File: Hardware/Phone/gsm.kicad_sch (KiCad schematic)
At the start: 28 parts

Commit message: e ink is done
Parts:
- removed U5: ~, Felix_GSM:GSMM-SMD_SIM800A32M, symbol Felix_GSM:SIM800A 32m
- added C24: 100n, Capacitor_SMD:C_0603_1608Metric, symbol Device:C
- added C25, C26, C27: 22p, Capacitor_SMD:C_0603_1608Metric, symbol Device:C
- added C28: 1u, Capacitor_SMD:C_0603_1608Metric, symbol Device:C
- added C29: 1nF, Capacitor_SMD:C_1206_3216Metric, symbol Device:C
- added C30, C31: ~, Capacitor_SMD:C_0603_1608Metric, symbol Device:C
- added CARD1: ~, Felix_GSM:SIM-SMD_503960-0696, symbol Felix_GSM:503960-0696
- added D5: ESDA6V1-5W6, Package_TO_SOT_SMD:SOT-363_SC-70-6, symbol Power_Protection:ESDA6V1-5SC6
- added D6: ~, Felix:SOD-882_L1.0-W0.6-BI, symbol Felix:H5VL10B
- added F2: 500mA PTC, Fuse:Fuse_1206_3216Metric_Pad1.42x1.75mm_HandSolder, symbol Device:Fuse
- added J5: Conn_Coaxial, Connector_Coaxial:U.FL_Hirose_U.FL-R-SMT-1_Vertical, symbol Connector:Conn_Coaxial
- added J6: Conn_01x02_Socket, Connector_PinHeader_2.54mm:PinHeader_1x02_P2.54mm_Vertical, symbol Connector:Conn_01x02_Socket
- added J7: USB_C_Receptacle_USB2.0_16P, Connector_USB:USB_C_Receptacle_HRO_TYPE-C-31-M-12, symbol Connector:USB_C_Receptacle_USB2.0_16P
- added R16, R18, R19: 1K, Resistor_SMD:R_0603_1608Metric, symbol Device:R
- added R17, R20: 5k6, Resistor_SMD:R_0603_1608Metric, symbol Device:R
- added R21: 4k7, Resistor_SMD:R_0603_1608Metric, symbol Device:R
- added R22, R23, R24: 51R, Resistor_SMD:R_0603_1608Metric, symbol Device:R
- added R25: 0R, Resistor_SMD:R_0603_1608Metric, symbol Device:R
- added TP1: TestPoint, TestPoint:TestPoint_Pad_D1.0mm, symbol Connector:TestPoint
- added U5: USBLC6-2SC6, Package_TO_SOT_SMD:SOT-23-6, symbol Power_Protection:USBLC6-2SC6
- added U6: SIM800C, RF_GSM:SIMCom_SIM800C, symbol RF_GSM:SIM800C
- added U7: ~, Felix:MIC-TH_BD4.0-P1.40_KEEG1542PBL-A, symbol Felix:KEEG1542PBL-A
- R11, R12: value 1K -> 22R
- R13: value 1K -> 5k1; footprint Resistor_SMD:R_0603_1608Metric -> Resistor_SMD:R_1206_3216Metric
- R14: value 5k6 -> 5k1; footprint Resistor_SMD:R_0603_1608Metric -> Resistor_SMD:R_1206_3216Metric
- R15: value 5k6 -> 1M; footprint Resistor_SMD:R_0603_1608Metric -> Resistor_SMD:R_1206_3216Metric
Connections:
- net +4V: now also U6.34 (VBAT), U6.35 (VBAT)
- net DTR: now also R16.2; no longer R13.2
- net GND: now also R13.2, C24.1, C25.1, C26.1, C27.1, C28.1, C29.2, C30.1, C31.1, CARD1.C5 (GND), CARD1.C9 (SHEEL), D5.2 (GND), D6.2 (A), J5.2 (Ext), J7.A1 (GND), J7.A12 (GND), J7.B1 (GND), J7.B12 (GND), R17.2, R20.2, U5.2 (GND), U6.13 (GND), U6.19 (GND), U6.21 (GND), U6.27 (GND), U6.30 (GND), U6.31 (GND), U6.33 (GND), U6.36 (GND), U6.37 (GND), U6.8 (GND)
- net RX: now also R19.2; no longer R12.2
- net TX: now also R18.2; no longer R11.2
- net at C20.1, C21.1, C22.2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: now also U6.10 (MICN), U7.1
- net at C18.1, C19.1, C20.2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: now also U6.9 (MICP), U7.2
- net at R13.1: now also J7.A5 (CC1); no longer R15.1
- net at C10.1, C11.2, C14.1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: now also J6.1 (Pin_1), U6.11 (SPKP)
- net at C10.2, C12.1, C13.1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: now also J6.2 (Pin_2), U6.12 (SPKN)
- net at R12.1: now also U5.3 (I/O2); no longer R14.1
- net at R11.1: now also U5.1 (I/O1)
- new net: R19.1, R20.1, U6.2 (UART1_RXD)
- new net: C28.2, F2.1, U5.5 (VBUS), U6.24 (USB_VBUS)
- new net: F2.2, J7.A4 (VBUS), J7.A9 (VBUS), J7.B4 (VBUS), J7.B9 (VBUS)
- new net: CARD1.C3 (CLK), D5.1 (IO1), R23.1
- new net: CARD1.C7 (I/O), D5.3 (IO2), R24.1
- new net: CARD1.C4 (DETECT), D5.4 (IO3), R21.2, U6.14 (SIM_DET)
- new net: CARD1.C2 (RST), D5.5 (IO4), R22.1
- new net: C24.2, CARD1.C1 (VCC), D5.6 (IO5), U6.18 (SIM_VDD)
- new net: C26.2, R23.2, U6.16 (SIM_CLK)
- new net: CARD1.C8 (DT-VSS), TP1.1
- new net: R12.2, U6.26 (USB_DM)
- new net: C31.2, D6.1 (C), J5.1 (In), R25.1
- new net: R16.1, R17.1, U6.6 (UART1_DTR)
- new net: C30.2, R25.2, U6.32 (GSM_ANT)
- new net: C27.2, R22.2, U6.17 (SIM_RST)
- new net: C25.2, R24.2, U6.15 (SIM_DATA)
- new net: J7.A7 (D-), J7.B7 (D-), U5.4 (I/O2)
- new net: J7.A6 (D+), J7.B6 (D+), U5.6 (I/O1)
- new net: R11.2, U6.25 (USB_DP)
- new net: R18.1, U6.1 (UART1_TXD)
- new net: J7.B5 (CC2), R14.1
- new net: C29.1, J7.S1 (SHIELD), R15.1
- new net: R21.1, U6.40 (VDD_EXT)
- new net PWRKEY: U6.39 (~{PWRKEY})
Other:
- moved on the sheet: C10, C11, C12, C13, C14, C15, C16, C17, C18, C19, C20, C21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

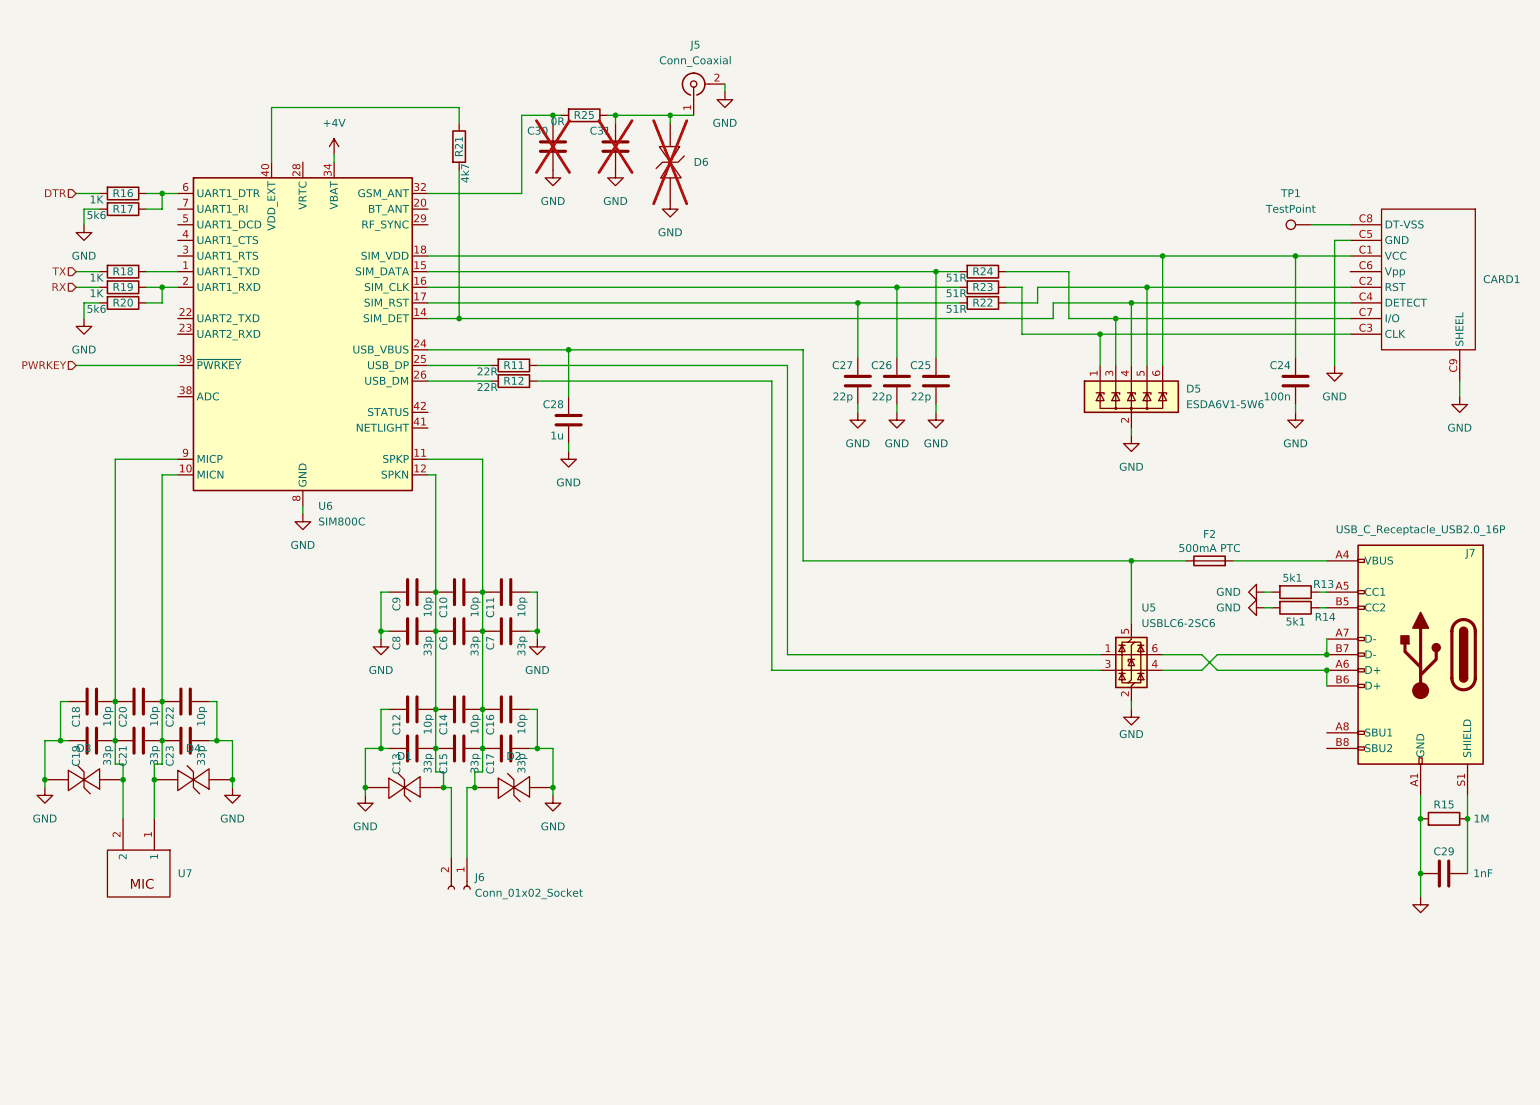
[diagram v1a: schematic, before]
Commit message: phone design is done abendoning projekt
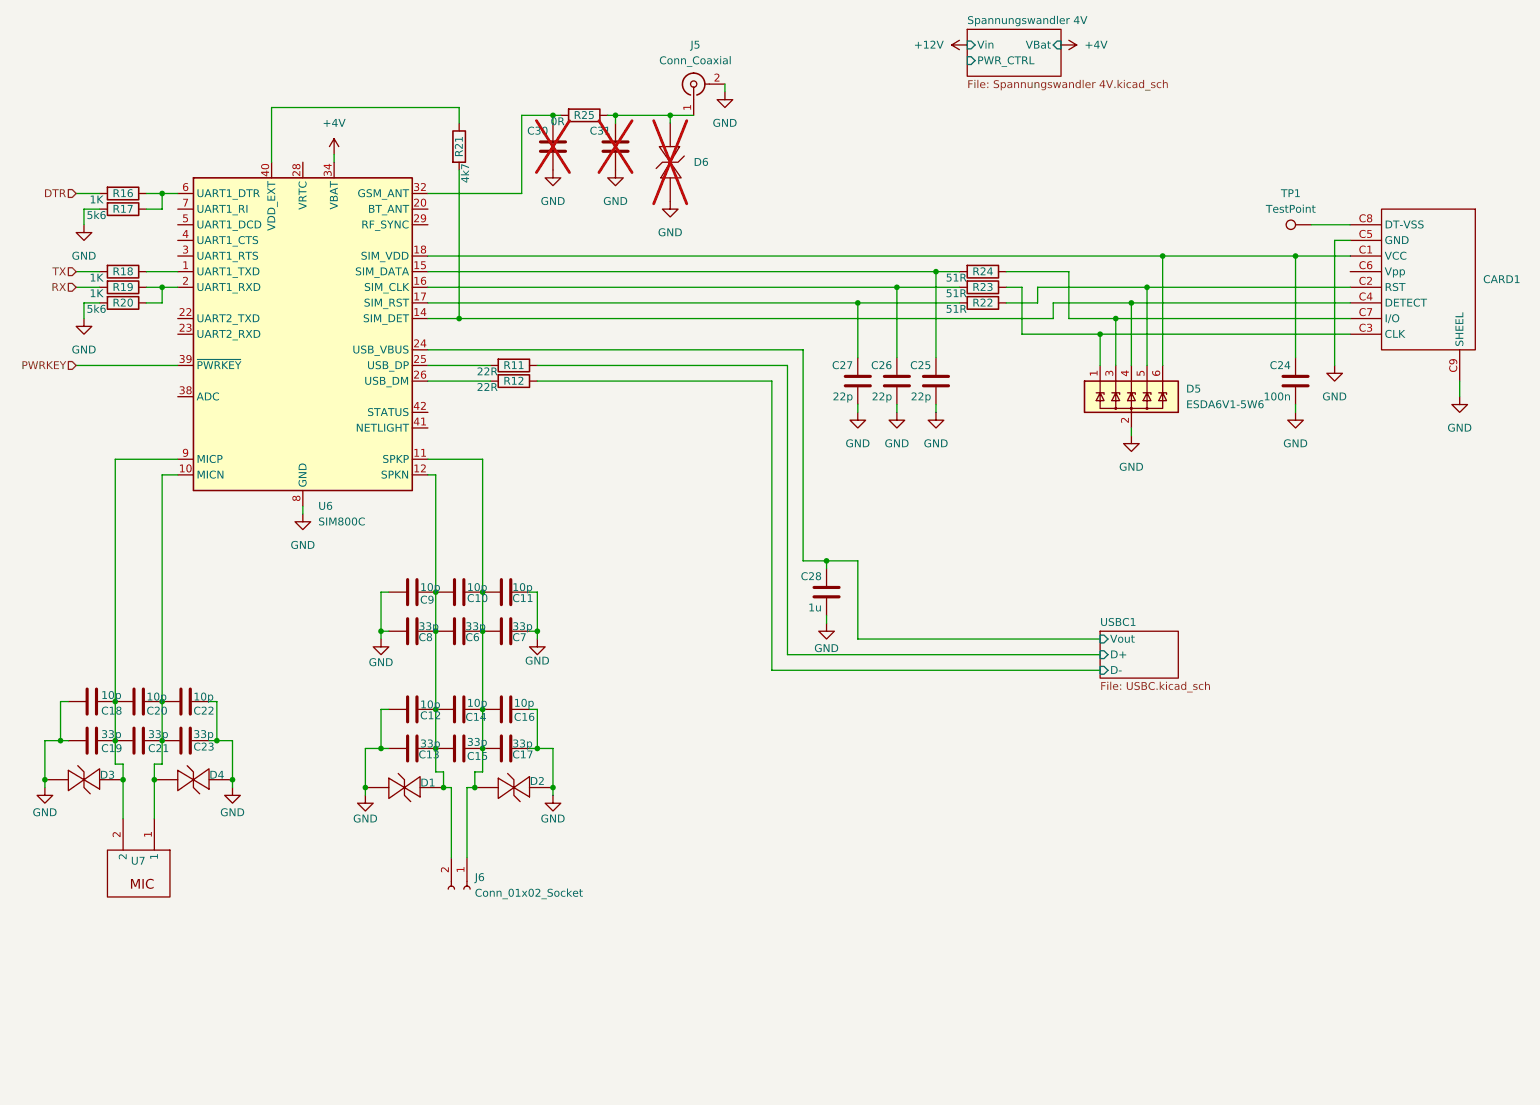
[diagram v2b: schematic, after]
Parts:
- removed C29: 1nF, Capacitor_SMD:C_1206_3216Metric, symbol Device:C
- removed F2: 500mA PTC, Fuse:Fuse_1206_3216Metric_Pad1.42x1.75mm_HandSolder, symbol Device:Fuse
- removed J7: USB_C_Receptacle_USB2.0_16P, Connector_USB:USB_C_Receptacle_HRO_TYPE-C-31-M-12, symbol Connector:USB_C_Receptacle_USB2.0_16P
- removed R13, R14: 5k1, Resistor_SMD:R_1206_3216Metric, symbol Device:R
- removed R15: 1M, Resistor_SMD:R_1206_3216Metric, symbol Device:R
- removed U5: USBLC6-2SC6, Package_TO_SOT_SMD:SOT-23-6, symbol Power_Protection:USBLC6-2SC6
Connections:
- net USBC1/Vout: now reaches C28.2, U6.24 (USB_VBUS)
- net USBC1/D-: now reaches R12.1
- net USBC1/D+: now reaches R11.1
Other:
- added sheet Spannungswandler 4V (Spannungswandler 4V.kicad_sch)
- added sheet USBC1 (USBC.kicad_sch)
- moved on the sheet: C28

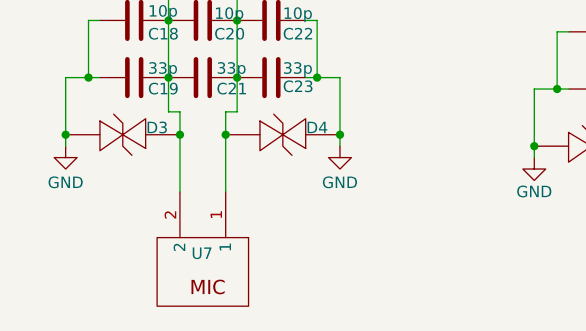
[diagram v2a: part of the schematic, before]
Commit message: added doku. Abendoning Projekt
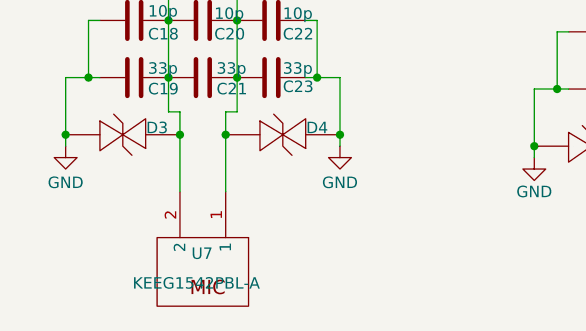
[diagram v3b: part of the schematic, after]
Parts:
- U7: value ~ -> KEEG1542PBL-A
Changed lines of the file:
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@@
 			)
 		)
-		(property "Value" "~"
+		(property "Value" " KEEG1542PBL-A"
 			(at 53.34 158.75 0)
 			(effects
